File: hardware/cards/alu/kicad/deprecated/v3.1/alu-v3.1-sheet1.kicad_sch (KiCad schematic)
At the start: 9 parts, among them IC1 74*04, IC2 74*240, IC3 74*244, IC4 74*00, IC5 74*374, IC6 74*08, IC7 74*32, IC8 74*138, IC9 74*74

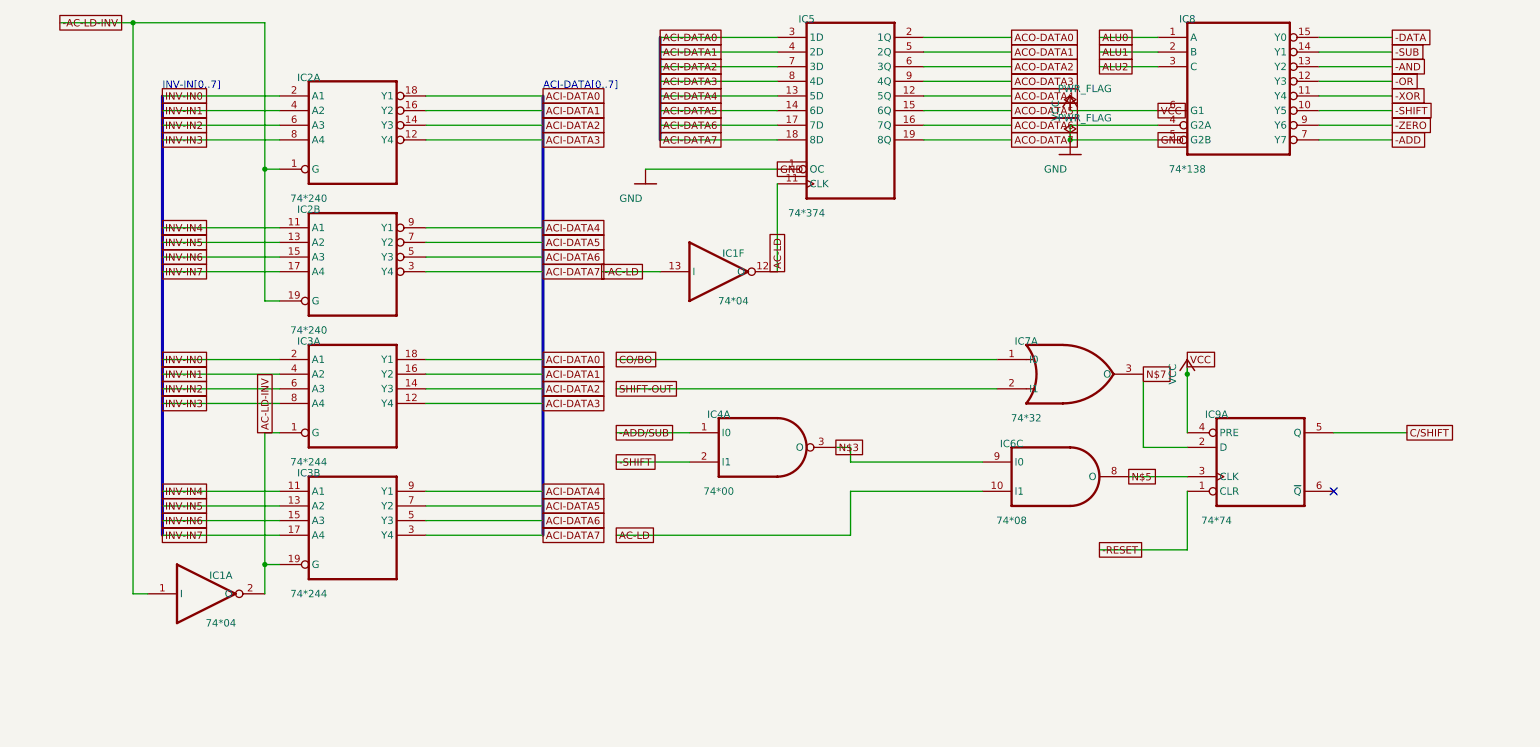
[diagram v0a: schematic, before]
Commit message: fix(kicad): readable converted schematics - overlaps 42,847 -> 3,147, nothing off the frame; CF sheet 0 overlaps
- tools/kicad/sch_overlaps.py: calibrated readability check (text/text, text/body, text/line, off frame/title block)
- eagle_sch_to_kicad.py: fields placed from Eagle's smashed attributes or the symbol's >NAME/>VALUE with Eagle's align,
  size and ratio, readable angles; fields Eagle never shows hidden (FABC96R shows only its pin name); pin numbers hidden
  where every Eagle pin hides them; Eagle-hidden layers dropped (the stray SpiceOrder text); labels on their own wires,
  converter labels only where KiCad needs them; rotate-then-mirror fixed for MR90/MR270 in pin_world/no-connects;
  each sheet on the smallest page that holds it, centred clear of the title block
- finish_board.py: stable footprint-library choice (DRC counts no longer vary run to run)
- all 37 projects regenerated: netlist proofs unchanged (34 MATCH, 2 schematic-only, video Fusion export MISMATCH as
  before); DRC same or better; ERC up (loose wire ends onto graphic buses no longer hidden by labels; explained per README)
- CF card: gate names off the gate bodies, U3 clear of its title, 5.08 mm connector pins; rebuilt: DRC 0/0, proof MATCH
- schematic PDFs regenerated (tools/sch_to_pdf.py, 37/37)

Co-Authored-By: Claude Opus 5.5 <noreply@anthropic.com>
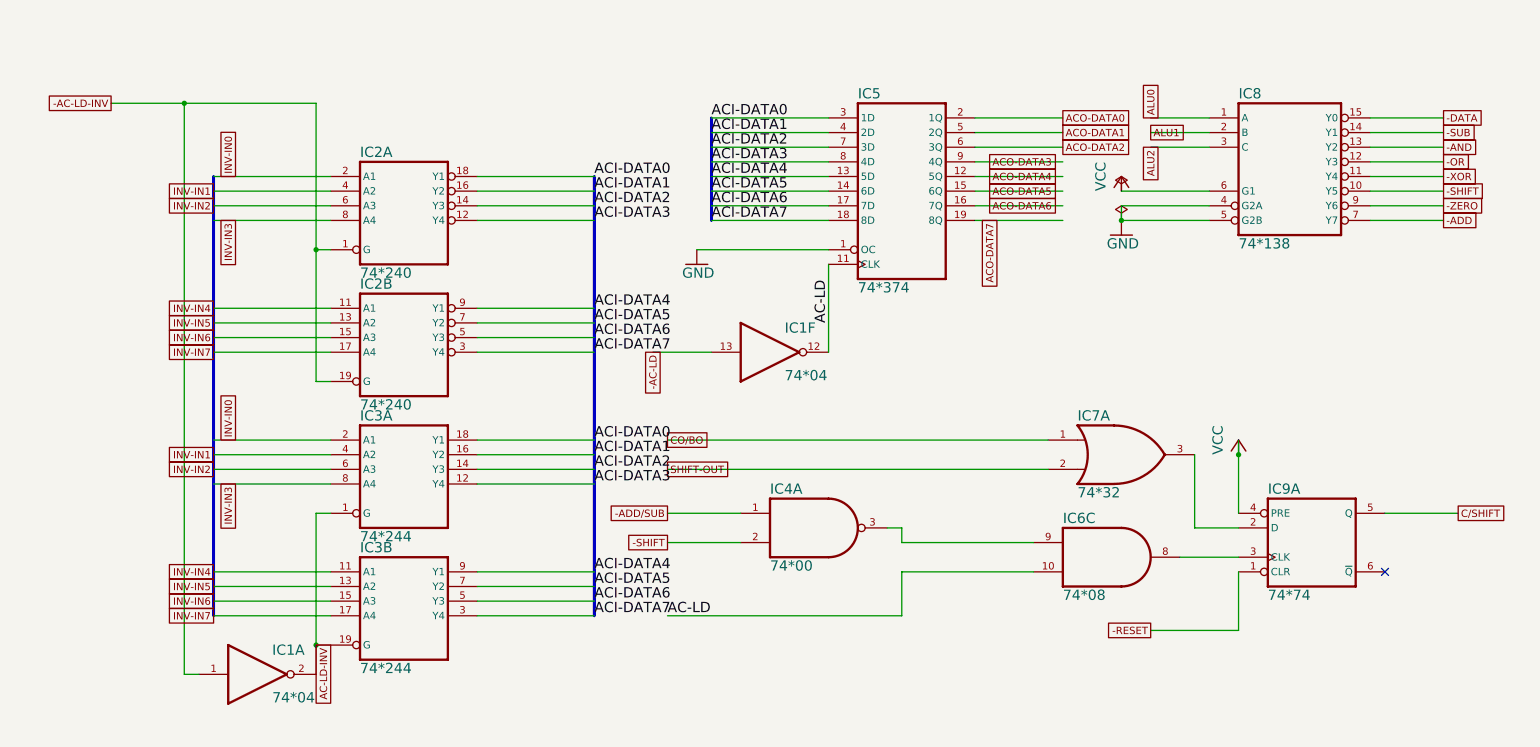
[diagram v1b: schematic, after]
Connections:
- net N$3: no longer names the net of IC4.3 (O), IC6.9 (I0)
- net N$5: no longer names the net of IC6.8 (O), IC9.3 (CLK)
- net N$7: no longer names the net of IC7.3 (O), IC9.2 (D)
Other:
- note removed: "ACI-DATA[0..7]"
- note removed: "INV-IN[0..7]"
- moved on the sheet: IC2A, IC2B, IC3A, IC3B, IC5, IC8, IC9A
